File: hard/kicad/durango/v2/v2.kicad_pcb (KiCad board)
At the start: 2 copper layers, 177.8 x 130.8 mm, 155 parts, among them J1 NANOLINK, J10 STEP, J11 EXPANSION, J2 AUDIO IN, J3 IOx, J4 LED, J605 COMPONENT VIDEO, J7 POWER IN, J706 COMPOSITE, J8 DEBUG, J9 CARTRIDGE, J905 SCART, Q1 BC548, Q2 BC548, Q3 BC548, Q307 BC548, Q4 BC548, Q5 BC548, Q608 BC548, Q609 BC548, Q610 BC548, Q611 BC548, Q906 BC548, SW1 RESET, SW2 NMI, U1 65C02, U10 74HC139, U104 74HC257, U105 74HC257, U11 74HC688, U12 74HC74, U124 74HC574, U125 74HC157, U126 74HC86, U127 74HC245, U13 74HC32, U14 74HC4040, U15 74HC4040, U16 74HC02, U17 74HC21, U18 74HC85, U19 CD4040, U20 74HC85, U204 74HC257, U205 74HC257, U22 74HC175, U224 74HC166, U227 74HC20, U23 74HC86, U29 74HC139, U3 62256, U31 74HC245, U32 74HC245, U321 74HC157, U428 74HC174, U530 74HC367, U6 74HC157, U7 74HC157, U8 74HC30, U9 74HC00, X1 28 MHz

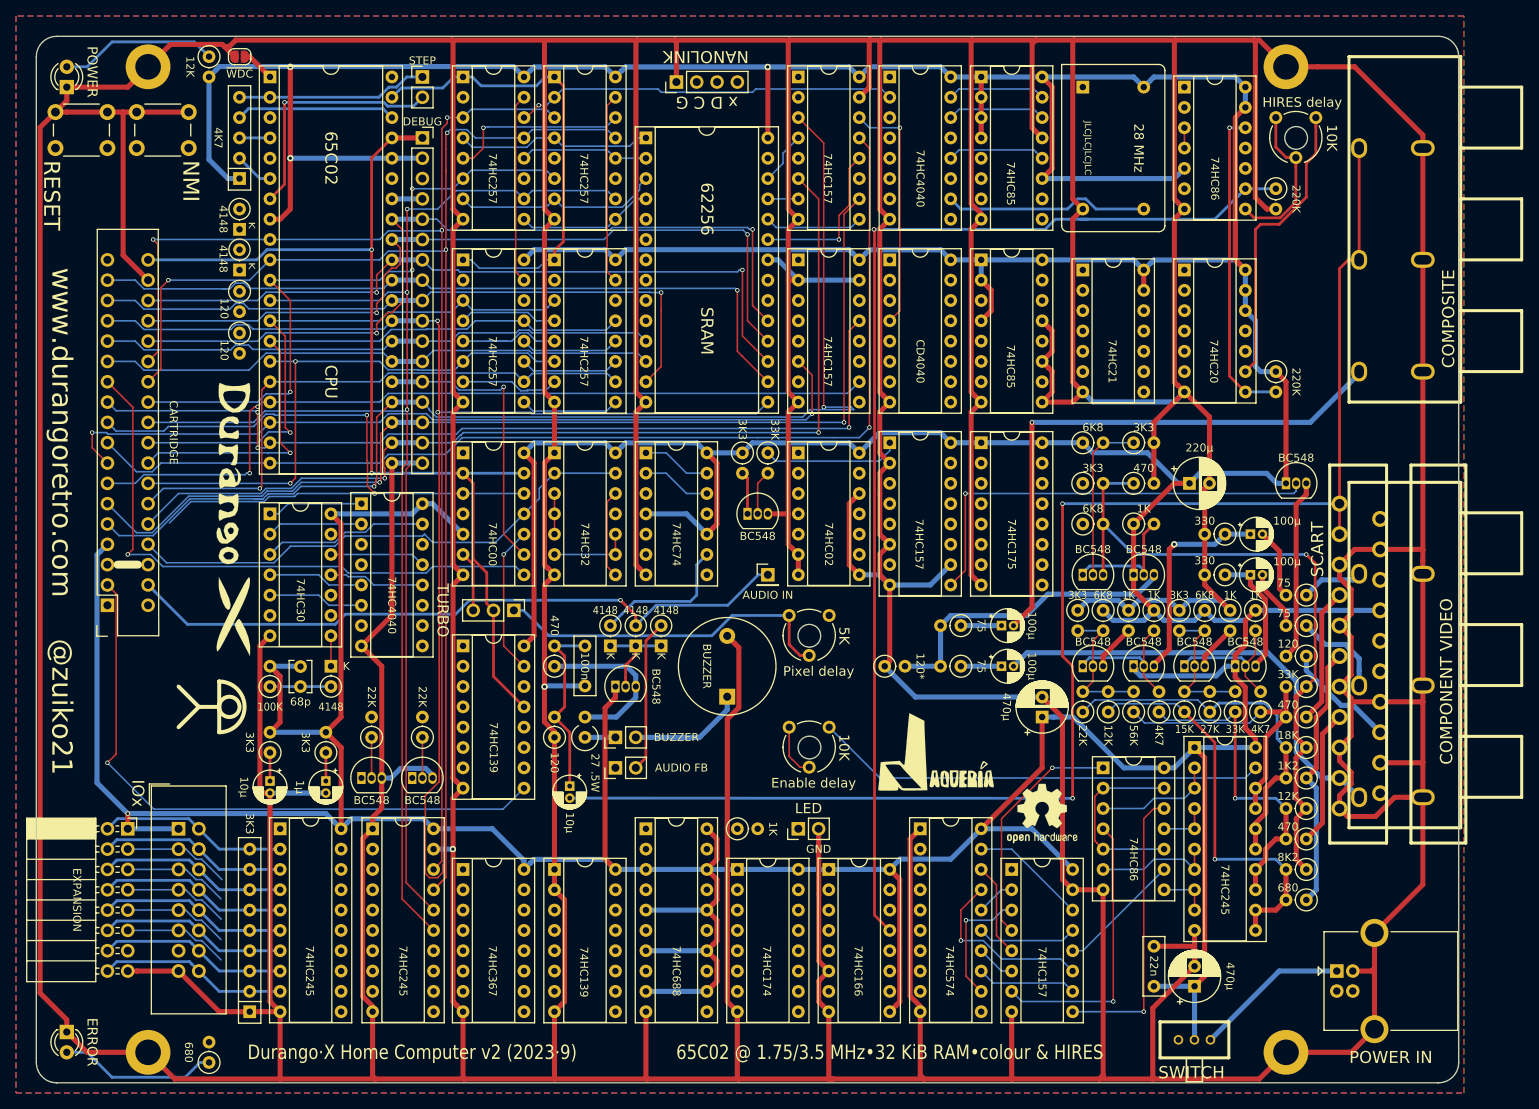
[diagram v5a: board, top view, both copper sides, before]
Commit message: interrupts and some muxed address lines
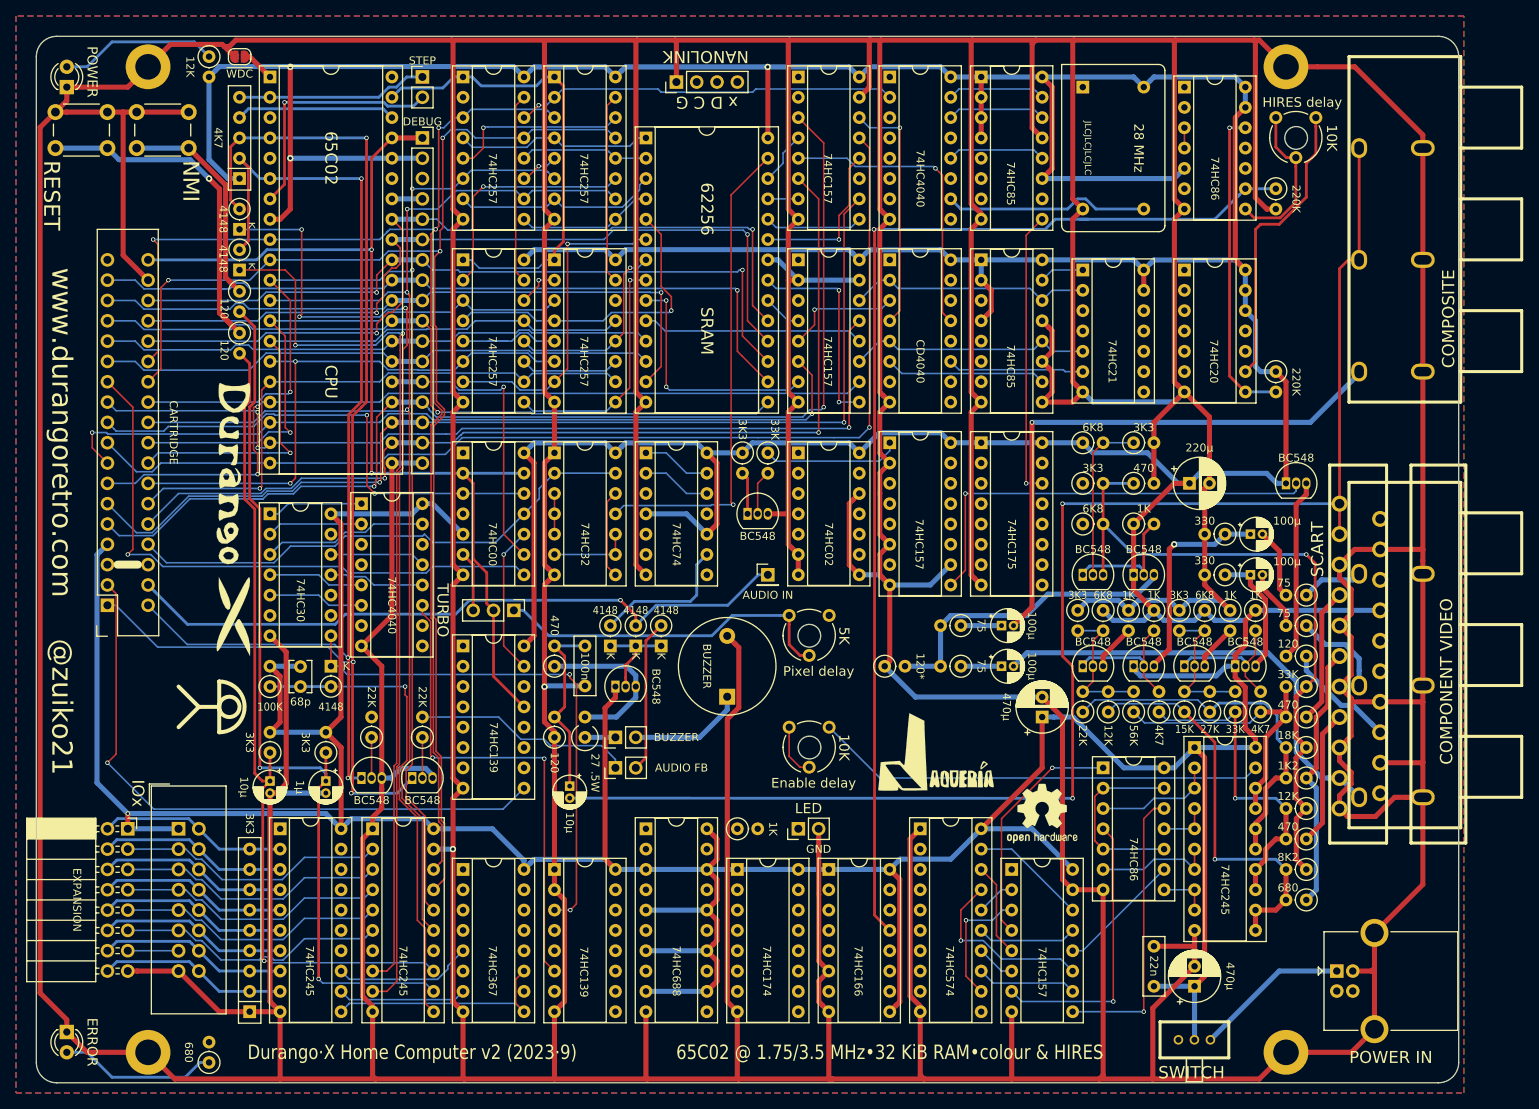
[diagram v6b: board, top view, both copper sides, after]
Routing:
- net ~IRQ: track 3.81 -> 150.7 mm, vias 0 -> 3
- net ~NMI: track 4.86 -> 133.7 mm, vias 0 -> 3
- net ~INTREQ: track 0.00 -> 120.8 mm, vias 0 -> 3
- net ~NMIREQ: track 0.00 -> 112.6 mm, vias 0 -> 2
- net /Power and Extras/~ANMI: track 3.56 -> 112.8 mm, vias 0 -> 2
- net /Power and Extras/~ARST: track 3.56 -> 104.3 mm, vias 0 -> 1
- net ~250HZ: track 3.81 -> 66.2 mm, vias 0 -> 2
- net /250HZ: track 0.00 -> 60.7 mm, vias 0 -> 2
- net /~DWE: track 0.00 -> 60.5 mm, vias 0 -> 1
- net D5: track 168.9 -> 112.3 mm, vias 2 -> 1
- net /Power and Extras/~ST250: track 7.62 -> 59.8 mm, vias 0 -> 1
- net /Power and Extras/R_SW: track 0.00 -> 43.0 mm, vias 0 -> 1
- net VA13: track 0.00 -> 37.5 mm, vias 0 -> 1
- net /Video & Clock generation/~VS: track 0.00 -> 35.8 mm, vias 0 -> 1
- net VA11: track 0.00 -> 30.6 mm
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
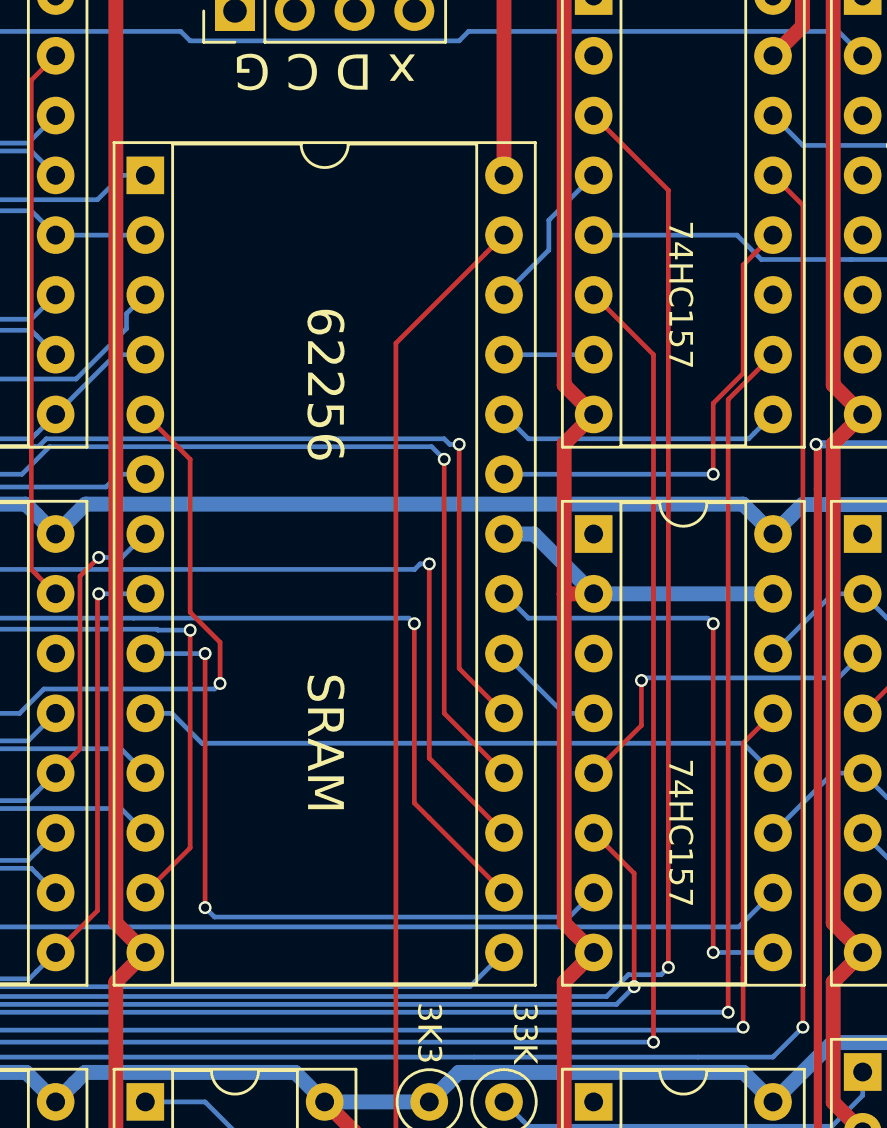
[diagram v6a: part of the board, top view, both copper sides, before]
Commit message: add narrow SRAM footprint
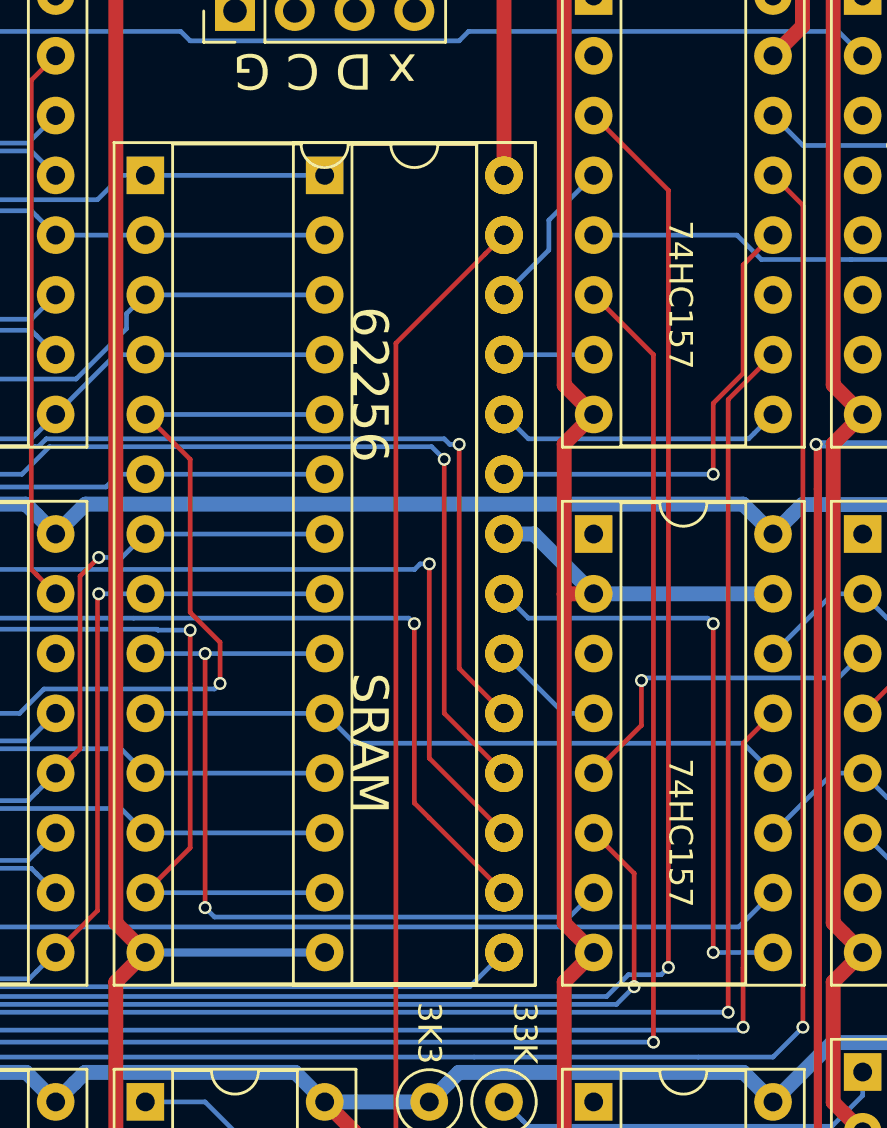
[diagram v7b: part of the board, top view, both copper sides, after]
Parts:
- added U003: 62256, Package_DIP:DIP-28_W7.62mm_Socket, F.Cu at (96.5, 25.4)
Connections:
- net /MA0 renamed MA0
- net /MA1 renamed MA1
- net /MA10 renamed MA10
- net /MA11 renamed MA11
- net /MA12 renamed MA12
- net /MA13 renamed MA13
- net /MA14 renamed MA14
- net /MA2 renamed MA2
- net /MA3 renamed MA3
- net /MA4 renamed MA4
- net /MA5 renamed MA5
- net /MA6 renamed MA6
- net /MA7 renamed MA7
- net /MA8 renamed MA8
- net /MA9 renamed MA9
- net /~DWE renamed ~DWE
- net /~MCS renamed ~MCS
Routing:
- net MA7: track 30.3 -> 38.0 mm
- net MA6: track 40.2 -> 47.8 mm
- net MA5: track 24.7 -> 32.3 mm
- net MA4: track 40.2 -> 47.8 mm
- net MA3: track 17.1 -> 24.8 mm
- net MA2: track 26.0 -> 33.6 mm
- net MA1: track 16.1 -> 23.7 mm
- net MA0: track 24.7 -> 32.3 mm
- net D7: track 99.9 -> 107.5 mm
- net D6: track 85.9 -> 93.5 mm
- net D4: track 83.1 -> 90.7 mm
- net GND: track 1963.1 -> 1970.8 mm
- net MA9: track 30.4 -> 35.5 mm

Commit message: some more signals
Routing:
- net VA0: track 0.00 -> 130.2 mm, vias 0 -> 1
- net /~IEN: track 0.00 -> 117.8 mm, vias 0 -> 1
- net VCLK: track 43.5 -> 118.5 mm, vias 0 -> 1
- net /Video & Clock generation/HVG: track 0.00 -> 68.3 mm, vias 0 -> 1
- net /IEN: track 0.00 -> 55.5 mm, vias 0 -> 1
- net /Video & Clock generation/DEV~ODD: track 0.00 -> 55.3 mm, vias 0 -> 1
- net /Video & Clock generation/~CDE: track 6.71 -> 59.7 mm, vias 0 -> 1
- net INVERT: track 23.7 -> 45.6 mm, vias 0 -> 1
- net /Video & Clock generation/~LOST: track 0.00 -> 20.2 mm
- net /Video & Clock generation/LATCH: track 0.00 -> 19.5 mm, vias 0 -> 1
- net /Video & Clock generation/UCDE: track 0.00 -> 13.5 mm
- net /Video & Clock generation/UHDE: track 0.00 -> 12.3 mm
- net /CNT1K: track 21.5 -> 25.6 mm
- net /CNT32: track 12.0 -> 13.0 mm
